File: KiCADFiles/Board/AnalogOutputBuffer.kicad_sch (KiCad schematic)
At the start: 15 parts, among them U1 OPA1655D

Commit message: chose all components
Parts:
- C15: footprint (none) -> PCM_SparkFun-Capacitor:C_0603_1608Metric; MPN (none) -> C0603C471J5GACTU
- C42: value 1.5n -> 1500p; footprint (none) -> PCM_SparkFun-Capacitor:C_0603_1608Metric; MPN (none) -> C0603C152F1GACTU
- C46: footprint (none) -> Capacitor_THT:CP_Radial_D5.0mm_P2.00mm; MPN (none) -> 50YXJ22MTA5X11
- C48: footprint (none) -> PCM_SparkFun-Capacitor:C_0603_1608Metric; MPN (none) -> GRM1885C1H682JA01D
- C50: value 10uF -> 10u; footprint ~ -> PCM_SparkFun-Capacitor:C_0805_2012Metric; MPN (none) -> CL21A106KAYNNNG; Voltage (none) -> 25V
- C51: footprint ~ -> PCM_SparkFun-Capacitor:C_0603_1608Metric; MPN (none) -> CL10B104KB8NNNL
- C9: footprint (none) -> PCM_SparkFun-Capacitor:C_0603_1608Metric; MPN (none) -> GRM1885C1H222JA01D
- FB7: value ${SIM.PARAMS} -> 220; footprint ~ -> Inductor_SMD:L_0603_1608Metric; MPN (none) -> MMZ1608B221CTAH0
- R18: footprint (none) -> PCM_SparkFun-Resistor:R_0805_2012Metric; MPN (none) -> ERA-6AEB4421V
- R20: footprint (none) -> PCM_SparkFun-Resistor:R_0805_2012Metric; MPN (none) -> ERA-6AEB1331V
- R22: footprint (none) -> PCM_SparkFun-Resistor:R_0805_2012Metric; MPN (none) -> RMCF0805FT2K32
- R23: value 715k -> 715; footprint (none) -> PCM_SparkFun-Resistor:R_0805_2012Metric; MPN (none) -> RC0805FR-07715RL
- R26: footprint (none) -> PCM_SparkFun-Resistor:R_0805_2012Metric; MPN (none) -> RG2012P-4991-B-T5
- R28: footprint (none) -> PCM_SparkFun-Resistor:R_0805_2012Metric; MPN (none) -> RC0805FR-071K5L
- U1: MPN (none) -> OPA1655D
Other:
- note added: "Output filter schematic copied from CS4272 datasheet Replaced original diff filter with single ended since cheaper"
- note removed: "Taken straight from datasheet for CS4272"
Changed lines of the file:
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@@
 		(company "RF William Hollender")
 	)
-	(text "Taken straight from datasheet for CS4272\n"
+	(text "Output filter schematic copied from CS4272 datasheet\nReplaced original diff filter with single ended since cheaper"
 		(exclude_from_sim no)
-		(at 159.512 69.85 0)
+		(at 150.368 73.914 0)
 		(effects
 			(font
@@
 			)
 		)
-		(property "Value" "10uF"
+		(property "Value" "10u"
 			(at 125.8824 44.069 0)
 			(effects
@@
 			)
 		)
-		(property "Footprint" "~"
+		(property "Footprint" "PCM_SparkFun-Capacitor:C_0805_2012Metric"
 			(at 126.6952 45.72 0)
 			(effects
@@
 			)
 		)
-		(property "MPN" ""
+		(property "MPN" "CL21A106KAYNNNG"
+			(at 125.73 41.91 0)
+			(effects
+				(font
+					(size 1.27 1.27)
+				)
+				(hide yes)
+			)
+		)
+		(property "Tol" ""
+			(at 125.73 41.91 0)
+			(effects
+				(font
+					(size 1.27 1.27)
+				)
+				(hide yes)
+			)
+		)
+		(property "Voltage" "25V"
 			(at 125.73 41.91 0)
 			(effects
@@
 			)
 		)
-		(property "Value" "1.5n"
+		(property "Value" "1500p"
 			(at 109.22 115.5635 0)
 			(effects
@@
 			)
 		)
-		(property "Footprint" ""
+		(property "Footprint" "PCM_SparkFun-Capacitor:C_0603_1608Metric"
 			(at 106.68 114.3 0)
 			(effects
@@
 			)
 		)
-		(property "MPN" ""
+		(property "MPN" "C0603C152F1GACTU"
+			(at 106.68 114.3 0)
+			(effects
+				(font
+					(size 1.27 1.27)
+				)
+				(hide yes)
+			)
+		)
+		(property "Tol" ""
 			(at 106.68 114.3 0)
 			(effects
@@
 			)
 		)
-		(property "Footprint" ""
+		(property "Footprint" "PCM_SparkFun-Resistor:R_0805_2012Metric"
 			(at 83.82 104.14 0)
 			(effects
@@
 			)
 		)
-		(property "MPN" ""
+		(property "MPN" "ERA-6AEB4421V"
+			(at 83.82 104.14 90)
+			(effects
+				(font
+					(size 1.27 1.27)
+				)
+				(hide yes)
+			)
+		)
+		(property "Tol" ""
 			(at 83.82 104.14 90)
 			(effects
@@
 			)
 		)
-		(property "Value" "715k"
+		(property "Value" "715"
 			(at 97.79 111.76 90)
 			(effects
@@
 			)
 		)
-		(property "Footprint" ""
+		(property "Footprint" "PCM_SparkFun-Resistor:R_0805_2012Metric"
 			(at 97.79 109.22 0)
 			(effects
@@
 			)
 		)
-		(property "MPN" ""
+		(property "MPN" "RC0805FR-07715RL"
+			(at 97.79 109.22 90)
+			(effects
+				(font
+					(size 1.27 1.27)
+				)
+				(hide yes)
+			)
+		)
+		(property "Tol" ""
 			(at 97.79 109.22 90)
 			(effects
@@
 			)
 		)
-		(property "Footprint" ""
+		(property "Footprint" "PCM_SparkFun-Resistor:R_0805_2012Metric"
 			(at 95.25 121.92 0)
 			(effects
@@
 			)
 		)
-		(property "MPN" ""
+		(property "MPN" "RC0805FR-071K5L"
+			(at 95.25 121.92 90)
+			(effects
+				(font
+					(size 1.27 1.27)
+				)
+				(hide yes)
+			)
+		)
+		(property "Tol" ""
 			(at 95.25 121.92 90)
 			(effects
@@
 			)
 		)
-		(property "Footprint" ""
+		(property "Footprint" "PCM_SparkFun-Resistor:R_0805_2012Metric"
 			(at 97.79 104.14 0)
 			(effects
@@
 			)
 		)
-		(property "MPN" ""
+		(property "MPN" "RMCF0805FT2K32"
+			(at 97.79 104.14 90)
+			(effects
+				(font
+					(size 1.27 1.27)
+				)
+				(hide yes)
+			)
+		)
+		(property "Tol" ""
 			(at 97.79 104.14 90)
 			(effects
@@
 			)
 		)
-		(property "Footprint" ""
+		(property "Footprint" "PCM_SparkFun-Resistor:R_0805_2012Metric"
 			(at 83.82 109.22 0)
 			(effects
@@
 			)
 		)
-		(property "MPN" ""
+		(property "MPN" "ERA-6AEB1331V"
+			(at 83.82 109.22 90)
+			(effects
+				(font
+					(size 1.27 1.27)
+				)
+				(hide yes)
+			)
+		)
+		(property "Tol" ""
 			(at 83.82 109.22 90)
 			(effects
@@
 			)
 		)
-		(property "Value" "${SIM.PARAMS}"
+		(property "Value" "220"
 			(at 106.68 35.56 0)
 			(effects
@@
 			)
 		)
-		(property "Footprint" "~"
+		(property "Footprint" "Inductor_SMD:L_0603_1608Metric"
 			(at 106.68 33.02 0)
 			(effects
@@
 			)
 		)
-		(property "MPN" ""
+		(property "MPN" "MMZ1608B221CTAH0 "
+			(at 106.68 33.02 0)
+			(effects
+				(font
+					(size 1.27 1.27)
+				)
+				(hide yes)
+			)
+		)
+		(property "Tol" ""
 			(at 106.68 33.02 0)
 			(effects
@@
 			)
 		)
-		(property "Footprint" ""
+		(property "Footprint" "PCM_SparkFun-Capacitor:C_0603_1608Metric"
 			(at 80.01 86.36 0)
 			(effects
@@
 			)
 		)
-		(property "MPN" ""
+		(property "MPN" "GRM1885C1H222JA01D"
+			(at 80.01 86.36 90)
+			(effects
+				(font
+					(size 1.27 1.27)
+				)
+				(hide yes)
+			)
+		)
+		(property "Tol" ""
 			(at 80.01 86.36 90)
 			(effects
@@
 			)
 		)
-		(property "Footprint" ""
+		(property "Footprint" "PCM_SparkFun-Capacitor:C_0603_1608Metric"
 			(at 115.57 92.71 0)
 			(effects
@@
 			)
 		)
-		(property "MPN" ""
+		(property "MPN" "C0603C471J5GACTU"
+			(at 115.57 92.71 90)
+			(effects
+				(font
+					(size 1.27 1.27)
+				)
+				(hide yes)
+			)
+		)
+		(property "Tol" ""
 			(at 115.57 92.71 90)
 			(effects
@@
 			)
 		)
-		(property "Footprint" ""
+		(property "Footprint" "PCM_SparkFun-Capacitor:C_0603_1608Metric"
 			(at 83.82 121.92 0)
 			(effects
@@
 			)
 		)
-		(property "MPN" ""
+		(property "MPN" "GRM1885C1H682JA01D"
+			(at 83.82 121.92 90)
+			(effects
+				(font
+					(size 1.27 1.27)
+				)
+				(hide yes)
+			)
+		)
+		(property "Tol" ""
 			(at 83.82 121.92 90)
 			(effects
@@
 			)
 		)
-		(property "Footprint" ""
+		(property "Footprint" "PCM_SparkFun-Resistor:R_0805_2012Metric"
 			(at 109.22 86.36 0)
 			(effects
@@
 			)
 		)
-		(property "MPN" ""
+		(property "MPN" "RG2012P-4991-B-T5"
+			(at 109.22 86.36 90)
+			(effects
+				(font
+					(size 1.27 1.27)
+				)
+				(hide yes)
+			)
+		)
+		(property "Tol" ""
 			(at 109.22 86.36 90)
 			(effects
@@
 			)
 		)
-		(property "Footprint" "~"
+		(property "Footprint" "PCM_SparkFun-Capacitor:C_0603_1608Metric"
 			(at 136.8552 45.72 0)
 			(effects
@@
 			)
 		)
-		(property "MPN" ""
+		(property "MPN" "CL10B104KB8NNNL"
+			(at 135.89 41.91 0)
+			(effects
+				(font
+					(size 1.27 1.27)
+				)
+				(hide yes)
+			)
+		)
+		(property "Tol" ""
 			(at 135.89 41.91 0)
 			(effects
@@
 			)
 		)
-		(property "MPN" ""
+		(property "MPN" "OPA1655D"
+			(at 118.11 106.68 0)
+			(effects
+				(font
+					(size 1.27 1.27)
+				)
+				(hide yes)
+			)
+		)
+		(property "Tol" ""
 			(at 118.11 106.68 0)
 			(effects
@@
 			)
 		)
-		(property "Footprint" ""
+		(property "Footprint" "Capacitor_THT:CP_Radial_D5.0mm_P2.00mm"
 			(at 101.6 121.92 0)
 			(effects
@@
 			)
 		)
-		(property "MPN" ""
+		(property "MPN" "50YXJ22MTA5X11"
 			(at 101.6 121.92 90)
 			(effects
+				(font
+					(size 1.27 1.27)
+				)
+				(hide yes)
+			)
+		)
+		(property "Tol" ""
+			(at 101.6 121.92 90)
+			(effects

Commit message: replaced sw with relay, routed line amp section
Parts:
- C15: footprint PCM_SparkFun-Capacitor:C_0603_1608Metric -> PCM_SparkFun-Capacitor:C_0805_2012Metric; MPN C0603C471J5GACTU -> 08053C471KAT2A
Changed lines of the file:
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@@
 			)
 		)
-		(property "Footprint" "PCM_SparkFun-Capacitor:C_0603_1608Metric"
+		(property "Footprint" "PCM_SparkFun-Capacitor:C_0805_2012Metric"
 			(at 115.57 92.71 0)
 			(effects
@@
 			)
 		)
-		(property "MPN" "C0603C471J5GACTU"
+		(property "MPN" "08053C471KAT2A "
 			(at 115.57 92.71 90)
 			(effects

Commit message: improved layout further
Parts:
- removed C46: 22u, Capacitor_THT:CP_Radial_D5.0mm_P2.00mm, symbol Device:C_Small_US
- added C44: 22u, Capacitor_SMD:C_0805_2012Metric_Pad1.18x1.45mm_HandSolder, symbol Device:C_Small
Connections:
- net GND: now also C44.1
- net at R28.2: now also C44.2
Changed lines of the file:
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@@
+	)
+	(symbol
+		(lib_id "Device:C_Small")
+		(at 101.6 121.92 270)
+		(unit 1)
+		(exclude_from_sim no)
+		(in_bom yes)
+		(on_board yes)
+		(dnp no)
+		(fields_autoplaced yes)
+		(property "Reference" "C44"
+			(at 101.5936 115.57 90)
+			(effects
+				(font
+					(size 1.27 1.27)
+				)
+			)
+		)
+		(property "Value" "22u"
+			(at 101.5936 118.11 90)
+			(effects
+				(font
+					(size 1.27 1.27)
+				)
+			)
+		)
+		(property "Footprint" "Capacitor_SMD:C_0805_2012Metric_Pad1.18x1.45mm_HandSolder"
+			(at 101.6 121.92 0)
+			(effects
+				(font
+					(size 1.27 1.27)
+				)
+				(hide yes)
+			)
+		)
+		(property "Datasheet" "~"
+			(at 101.6 121.92 0)
+			(effects
+				(font
+					(size 1.27 1.27)
+				)
+				(hide yes)
+			)
+		)
+		(property "Description" "Unpolarized capacitor, small symbol"
+			(at 101.6 121.92 0)
+			(effects
+				(font
+					(size 1.27 1.27)
+				)
+				(hide yes)
+			)
+		)
+		(property "MPN" "KAM21AT70J226MU"
+			(at 101.6 121.92 0)
+			(effects
+				(font
+					(size 1.27 1.27)
+				)
+				(hide yes)
+			)
+		)
+		(property "Tol" ""
+			(at 101.6 121.92 0)
+			(effects
+				(font
+					(size 1.27 1.27)
+				)
+				(hide yes)
+			)
+		)
+		(pin "2"
+		)
+		(pin "1"
+		)
+		(instances
+			(project "SuperAudioBoard"
+				(path "/01f65e03-4e05-4001-87b4-b3e88e4198ab/00000000-0000-0000-0000-00005438c479/00000000-0000-0000-0000-0000545aeac8"
+					(reference "C46")
+					(unit 1)
+				)
+				(path "/01f65e03-4e05-4001-87b4-b3e88e4198ab/00000000-0000-0000-0000-00005438c479/00000000-0000-0000-0000-0000545b0a21"
+					(reference "C44")
+					(unit 1)
+				)
+			)
+		)
 	)
 	(symbol
@@
 					(unit 1)
 				)
-			)
-		)
-	)
-	(symbol
-		(lib_id "Device:C_Small_US")
-		(at 101.6 121.92 90)
-		(mirror x)
-		(unit 1)
-		(exclude_from_sim no)
-		(in_bom yes)
-		(on_board yes)
-		(dnp no)
-		(property "Reference" "C46"
-			(at 101.727 128.27 90)
-			(effects
-				(font
-					(size 1.27 1.27)
-				)
-			)
-		)
-		(property "Value" "22u"
-			(at 101.727 125.73 90)
-			(effects
-				(font
-					(size 1.27 1.27)
-				)
-			)
-		)
-		(property "Footprint" "Capacitor_THT:CP_Radial_D5.0mm_P2.00mm"
-			(at 101.6 121.92 0)
-			(effects
-				(font
-					(size 1.27 1.27)
-				)
-				(hide yes)
-			)
-		)
-		(property "Datasheet" ""
-			(at 101.6 121.92 0)
-			(effects
-				(font
-					(size 1.27 1.27)
-				)
-				(hide yes)
-			)
-		)
-		(property "Description" "capacitor, small US symbol"
-			(at 101.6 121.92 0)
-			(effects
-				(font
-					(size 1.27 1.27)
-				)
-				(hide yes)
-			)
-		)
-		(property "MPN" "50YXJ22MTA5X11"
-			(at 101.6 121.92 90)
-			(effects
-				(font
-					(size 1.27 1.27)
-				)
-				(hide yes)
-			)
-		)
-		(property "Tol" ""
-			(at 101.6 121.92 90)
-			(effects
-				(font
-					(size 1.27 1.27)
-				)
-				(hide yes)
-			)
-		)
-		(pin "1"
-		)
-		(pin "2"
-		)
-		(instances
-			(project ""
-				(path "/01f65e03-4e05-4001-87b4-b3e88e4198ab/00000000-0000-0000-0000-00005438c479/00000000-0000-0000-0000-0000545aeac8"
-					(reference "C47")
-					(unit 1)
-				)
-				(path "/01f65e03-4e05-4001-87b4-b3e88e4198ab/00000000-0000-0000-0000-00005438c479/00000000-0000-0000-0000-0000545b0a21"
-					(reference "C46")
-					(unit 1)
-				)

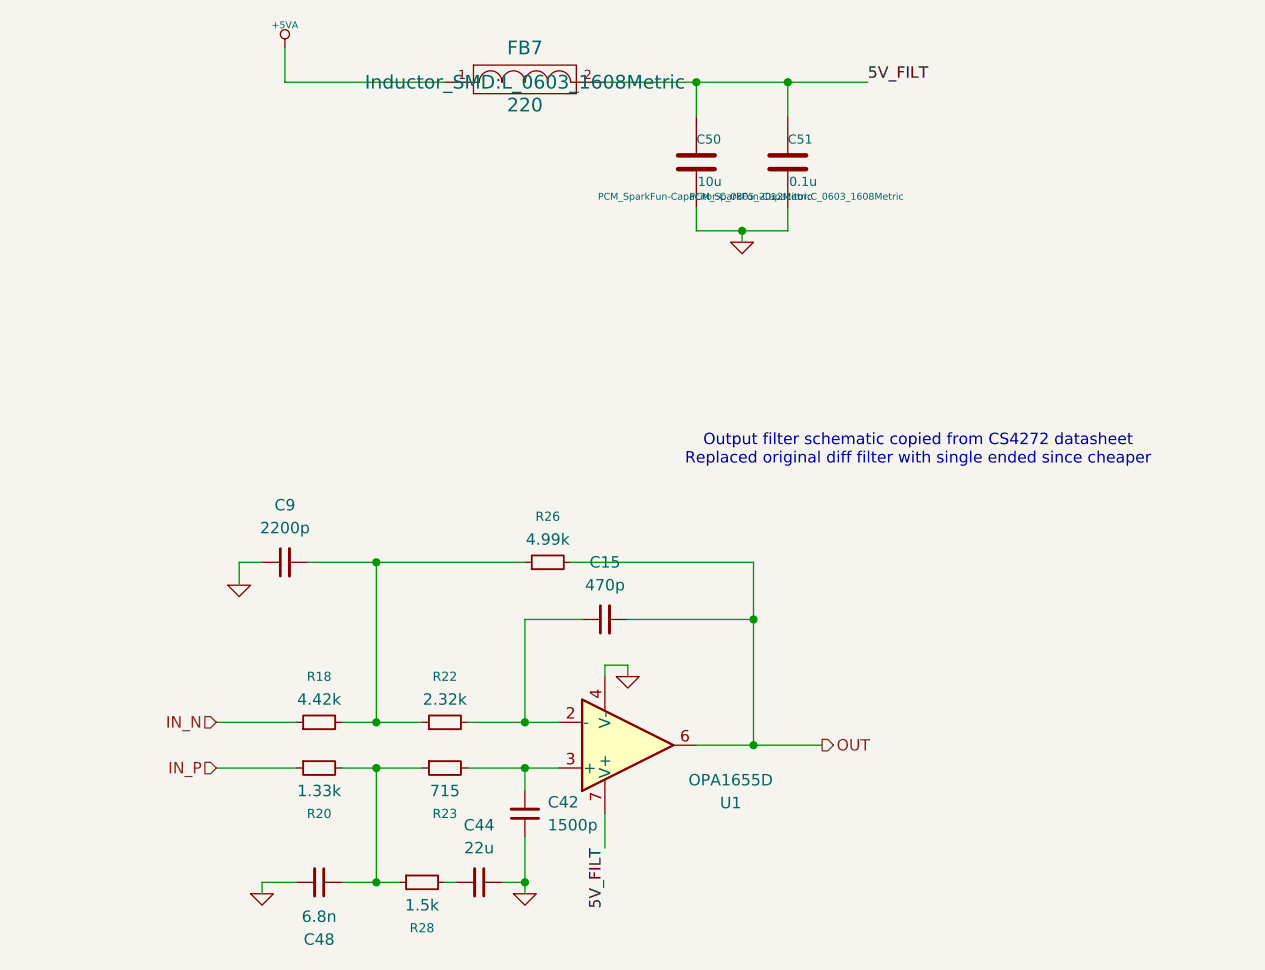
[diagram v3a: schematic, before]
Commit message: finished layout, passed DRC
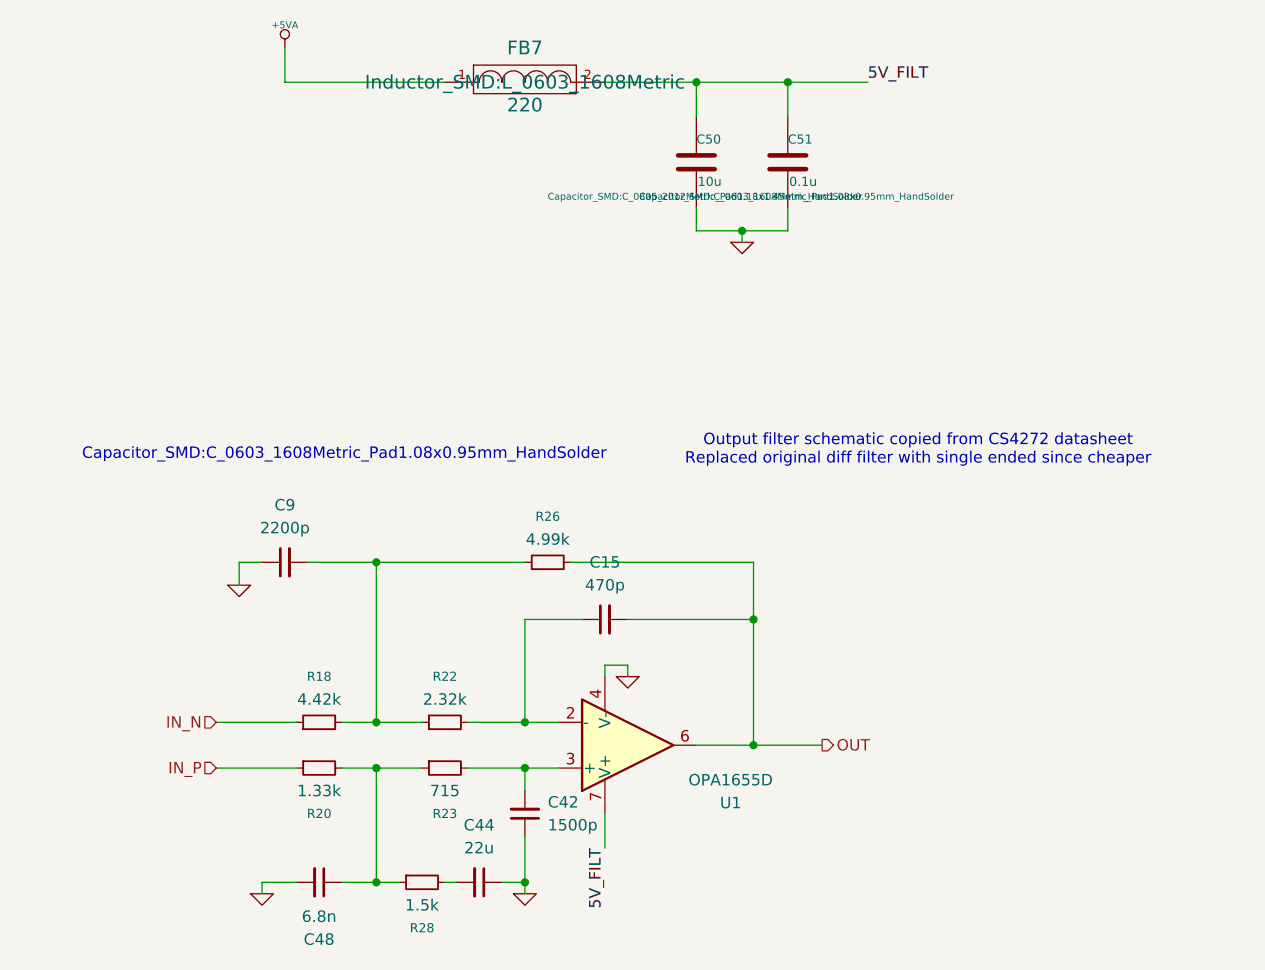
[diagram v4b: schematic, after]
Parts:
- C15: footprint PCM_SparkFun-Capacitor:C_0805_2012Metric -> Capacitor_SMD:C_0603_1608Metric_Pad1.08x0.95mm_HandSolder
- C42, C48, C51, C9: footprint PCM_SparkFun-Capacitor:C_0603_1608Metric -> Capacitor_SMD:C_0603_1608Metric_Pad1.08x0.95mm_HandSolder
- C50: footprint PCM_SparkFun-Capacitor:C_0805_2012Metric -> Capacitor_SMD:C_0805_2012Metric_Pad1.18x1.45mm_HandSolder
- R18, R20, R22, R23, R26, R28: footprint PCM_SparkFun-Resistor:R_0805_2012Metric -> Resistor_SMD:R_0805_2012Metric
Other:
- note added: "Capacitor_SMD:C_0603_1608Metric_Pad1.08x0.95mm_HandSolder"
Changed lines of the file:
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@@
 		(company "RF William Hollender")
+	)
+	(text "Capacitor_SMD:C_0603_1608Metric_Pad1.08x0.95mm_HandSolder"
+		(exclude_from_sim no)
+		(at 86.614 74.422 0)
+		(effects
+			(font
+				(size 1.27 1.27)
+			)
+		)
 	)
 	(text "Output filter schematic copied from CS4272 datasheet\nReplaced original diff filter with single ended since cheaper"
@@
 			)
 		)
-		(property "Footprint" "PCM_SparkFun-Capacitor:C_0805_2012Metric"
+		(property "Footprint" "Capacitor_SMD:C_0805_2012Metric_Pad1.18x1.45mm_HandSolder"
 			(at 126.6952 45.72 0)
 			(effects
@@
 			)
 		)
-		(property "Footprint" "PCM_SparkFun-Capacitor:C_0603_1608Metric"
+		(property "Footprint" "Capacitor_SMD:C_0603_1608Metric_Pad1.08x0.95mm_HandSolder"
 			(at 106.68 114.3 0)
 			(effects
@@
 			)
 		)
-		(property "Footprint" "PCM_SparkFun-Resistor:R_0805_2012Metric"
+		(property "Footprint" "Resistor_SMD:R_0805_2012Metric"
 			(at 83.82 104.14 0)
 			(effects
@@
 			)
 		)
-		(property "Footprint" "PCM_SparkFun-Resistor:R_0805_2012Metric"
+		(property "Footprint" "Resistor_SMD:R_0805_2012Metric"
 			(at 97.79 109.22 0)
 			(effects
@@
 			)
 		)
-		(property "Footprint" "PCM_SparkFun-Resistor:R_0805_2012Metric"
+		(property "Footprint" "Resistor_SMD:R_0805_2012Metric"
 			(at 95.25 121.92 0)
 			(effects
@@
 			)
 		)
-		(property "Footprint" "PCM_SparkFun-Resistor:R_0805_2012Metric"
+		(property "Footprint" "Resistor_SMD:R_0805_2012Metric"
 			(at 97.79 104.14 0)
 			(effects
@@
 			)
 		)
-		(property "Footprint" "PCM_SparkFun-Resistor:R_0805_2012Metric"
+		(property "Footprint" "Resistor_SMD:R_0805_2012Metric"
 			(at 83.82 109.22 0)
 			(effects
@@
 			)
 		)
-		(property "Footprint" "PCM_SparkFun-Capacitor:C_0603_1608Metric"
+		(property "Footprint" "Capacitor_SMD:C_0603_1608Metric_Pad1.08x0.95mm_HandSolder"
 			(at 80.01 86.36 0)
 			(effects
@@
 			)
 		)
-		(property "Footprint" "PCM_SparkFun-Capacitor:C_0805_2012Metric"
+		(property "Footprint" "Capacitor_SMD:C_0603_1608Metric_Pad1.08x0.95mm_HandSolder"
 			(at 115.57 92.71 0)
 			(effects
@@
 			)
 		)
-		(property "Footprint" "PCM_SparkFun-Capacitor:C_0603_1608Metric"
+		(property "Footprint" "Capacitor_SMD:C_0603_1608Metric_Pad1.08x0.95mm_HandSolder"
 			(at 83.82 121.92 0)
 			(effects
@@
 			)
 		)
-		(property "Footprint" "PCM_SparkFun-Resistor:R_0805_2012Metric"
+		(property "Footprint" "Resistor_SMD:R_0805_2012Metric"
 			(at 109.22 86.36 0)
 			(effects
@@
 			)
 		)
-		(property "Footprint" "PCM_SparkFun-Capacitor:C_0603_1608Metric"
+		(property "Footprint" "Capacitor_SMD:C_0603_1608Metric_Pad1.08x0.95mm_HandSolder"
 			(at 136.8552 45.72 0)
 			(effects
